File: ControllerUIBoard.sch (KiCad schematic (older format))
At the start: 27 parts, among them J11 KeySwitch, J6 ATMEGA_PROG, J7 SignalStrength, J8 UIBoardCON1, Q1 BSS314PEH6327XTSA1, U1 ATmega4809-A

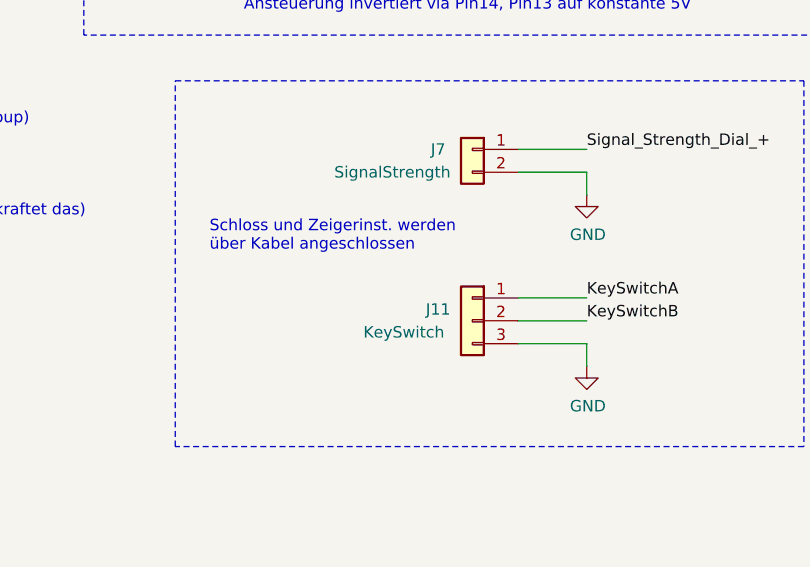
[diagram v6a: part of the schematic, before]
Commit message: - vorlaeufige Bauteil Positionierung
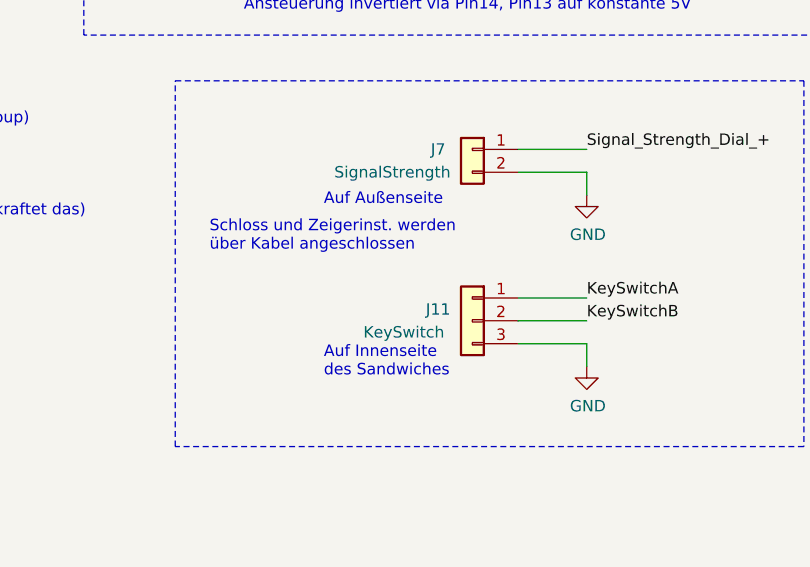
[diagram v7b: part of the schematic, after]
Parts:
- J6: footprint Connector_PinHeader_2.54mm:PinHeader_1x03_P2.54mm_Vertical -> Connector_PinHeader_2.54mm:PinHeader_1x03_P2.54mm_Horizontal
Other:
- note added: "Auf Außenseite"
- note added: "Auf Innenseite \ndes Sandwiches"
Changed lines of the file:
@@
 F 0 "J6" H 5650 7000 50  0000 C CNN
 F 1 "ATMEGA_PROG" H 5850 6900 50  0000 C CNN
-F 2 "Connector_PinHeader_2.54mm:PinHeader_1x03_P2.54mm_Vertical" H 5500 6950 50  0001 C CNN
+F 2 "Connector_PinHeader_2.54mm:PinHeader_1x03_P2.54mm_Horizontal" H 5500 6950 50  0001 C CNN
 F 3 "~" H 5500 6950 50  0001 C CNN
 	1    5500 6950
@@
 Wire Notes Line
 	7400 4600 7400 2750
+Text Notes 8450 5350 0    50   ~ 0
+Auf Außenseite
+Text Notes 8450 6100 0    50   ~ 0
+Auf Innenseite \ndes Sandwiches
 $EndSCHEMATC

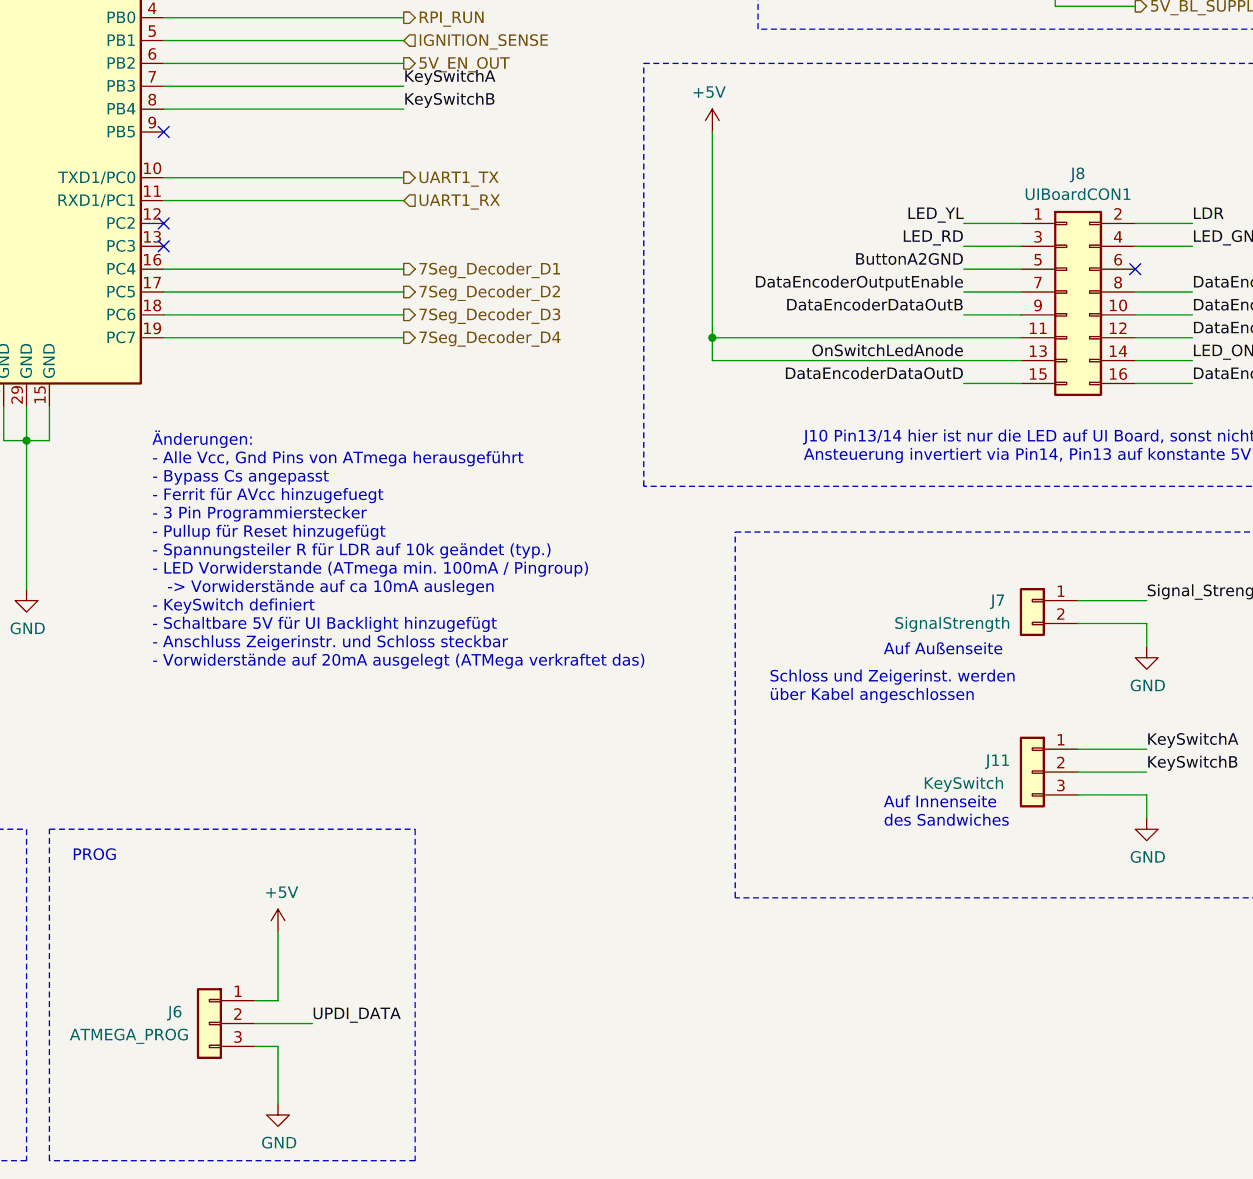
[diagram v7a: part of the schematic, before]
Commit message: - neue Stecker hinzugefügt, Annotation überall entsprechend angepasst Footprint fehlt noch
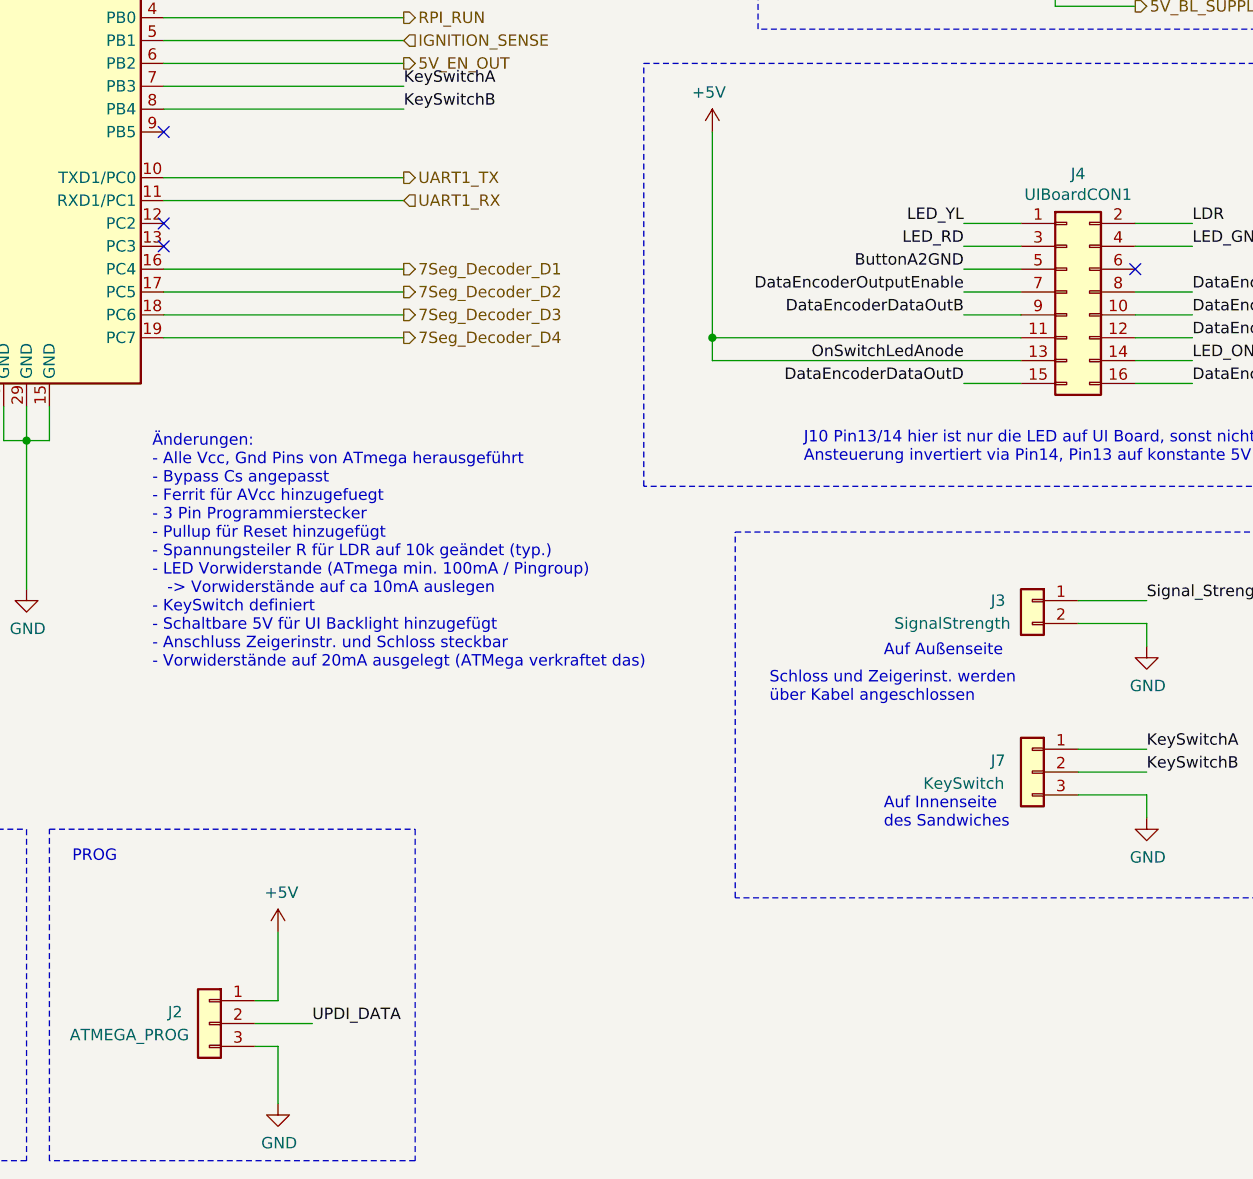
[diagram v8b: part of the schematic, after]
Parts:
- renumbered J6 to J2, J7 to J3, J8 to J4, J11 to J7
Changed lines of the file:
@@
 AR Path="/6205CD91" Ref="J?"  Part="1"
 AR Path="/60F87146/6205CD91" Ref="J?"  Part="1"
-AR Path="/60F18E7A/6205CD91" Ref="J8"  Part="1"
-F 0 "J8" H 9300 4267 50  0000 C CNN
+AR Path="/60F18E7A/6205CD91" Ref="J4"  Part="1"
+F 0 "J4" H 9300 4267 50  0000 C CNN
 F 1 "UIBoardCON1" H 9300 4176 50  0000 C CNN
 F 2 "Connector_PinSocket_2.54mm:PinSocket_2x08_P2.54mm_Vertical" H 9250 3750 50  0001 C CNN
@@
 BLM18AG471SN1D
 $Comp
-L Connector_Generic:Conn_01x03 J6
+L Connector_Generic:Conn_01x03 J2
 U 1 1 60FF9EA7
 P 5500 6950
-F 0 "J6" H 5650 7000 50  0000 C CNN
+F 0 "J2" H 5650 7000 50  0000 C CNN
 F 1 "ATMEGA_PROG" H 5850 6900 50  0000 C CNN
 F 2 "Connector_PinHeader_2.54mm:PinHeader_1x03_P2.54mm_Horizontal" H 5500 6950 50  0001 C CNN
@@
 	3800 1100 3800 950
 $Comp
-L Connector_Generic:Conn_01x02 J7
+L Connector_Generic:Conn_01x02 J3
 U 1 1 6103284D
 P 9100 5100
-F 0 "J7" H 9250 5100 50  0000 C CNN
+F 0 "J3" H 9250 5100 50  0000 C CNN
 F 1 "SignalStrength" H 9450 5000 50  0000 C CNN
 F 2 "Connector_Molex:Molex_PicoBlade_53048-0210_1x02_P1.25mm_Horizontal" H 9100 5100 50  0001 C CNN
@@
 	7900 2600 7900 1150
 $Comp
-L Connector_Generic:Conn_01x03 J11
+L Connector_Generic:Conn_01x03 J7
 U 1 1 6182A98D
 P 9100 5850
-F 0 "J11" H 9250 5900 50  0000 C CNN
+F 0 "J7" H 9250 5900 50  0000 C CNN
 F 1 "KeySwitch" H 9400 5800 50  0000 C CNN
 F 2 "Connector_Molex:Molex_PicoBlade_53048-0310_1x03_P1.25mm_Horizontal" H 9100 5850 50  0001 C CNN
